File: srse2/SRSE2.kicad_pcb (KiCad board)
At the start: 2 copper layers, 82 x 72 mm, 82 parts, among them J1 s88-N, J2 CAN, P1 I2S, P10 PIC_SPARE, P11 RS485 TERM, P12 RS485, P13 CONN_01X03, P14 CONN_01X04, P15 S88I, P16 CONN_01X04, P17 RA5, P18 CONN_01X03, P19 CONN_01X02, P2 CONN_01X09, P3 CONN_01X02, P4 CONN_01X04, P5 CONN_01X04, P6 ISO_I2C, P7 CAN_TERM, P8 CAN, P9 PIC_I2C, U1 Omega2, U10 OKI-78SR, U2 ADuM1250, U3 MCP2562, U4 PIC18F25K80, U5 HR911105A, U6 SP3485, U8 4504, U9 7812, Y1 16MHz

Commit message: add bulge
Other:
- outline, holes or cut-outs redrawn
- board text added: "V1.5"
- board text removed: "V1.4"
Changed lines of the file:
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@@
-(kicad_pcb (version 4) (host pcbnew 4.0.2+dfsg1-stable)
+(kicad_pcb (version 4) (host pcbnew 4.0.7)
   (general
     (links 208)
     (no_connects 0)
-    (area 97.888667 73.924999 207 154.126)
+    (area 97.963667 73.924999 206.85 154.286)
     (thickness 1.6)
-    (drawings 53)
+    (drawings 56)
     (tracks 1381)
     (zones 0)
@@
     )
   )
+  (gr_arc (start 141 146) (end 141 144) (angle 90) (layer Edge.Cuts) (width 0.15))
+  (gr_arc (start 141 146) (end 139 146) (angle 90) (layer Edge.Cuts) (width 0.15))
+  (gr_line (start 170 146) (end 143 146) (angle 90) (layer Edge.Cuts) (width 0.15))
   (gr_line (start 170 144) (end 170 146) (angle 90) (layer Edge.Cuts) (width 0.15))
   (gr_arc (start 182 144) (end 170 144) (angle 90) (layer Edge.Cuts) (width 0.15))
@@
     (effects (font (size 1 1) (thickness 0.2)))
   )
-  (gr_text V1.4 (at 162.2425 76.0095) (layer F.Cu)
+  (gr_text V1.5 (at 162.2425 76.0095) (layer F.Cu)
     (effects (font (size 1.5 1.5) (thickness 0.3)))
   )
@@
   (gr_line (start 100 86) (end 100 132) (angle 90) (layer Edge.Cuts) (width 0.15))
   (gr_line (start 182 86) (end 182 132) (angle 90) (layer Edge.Cuts) (width 0.15))
-  (gr_line (start 112 146) (end 170 146) (angle 90) (layer Edge.Cuts) (width 0.15))
+  (gr_line (start 112 146) (end 139 146) (angle 90) (layer Edge.Cuts) (width 0.15))
   (gr_arc (start 182 74) (end 182 86) (angle 90) (layer Edge.Cuts) (width 0.15))
   (gr_arc (start 100 74) (end 112 74) (angle 90) (layer Edge.Cuts) (width 0.15))

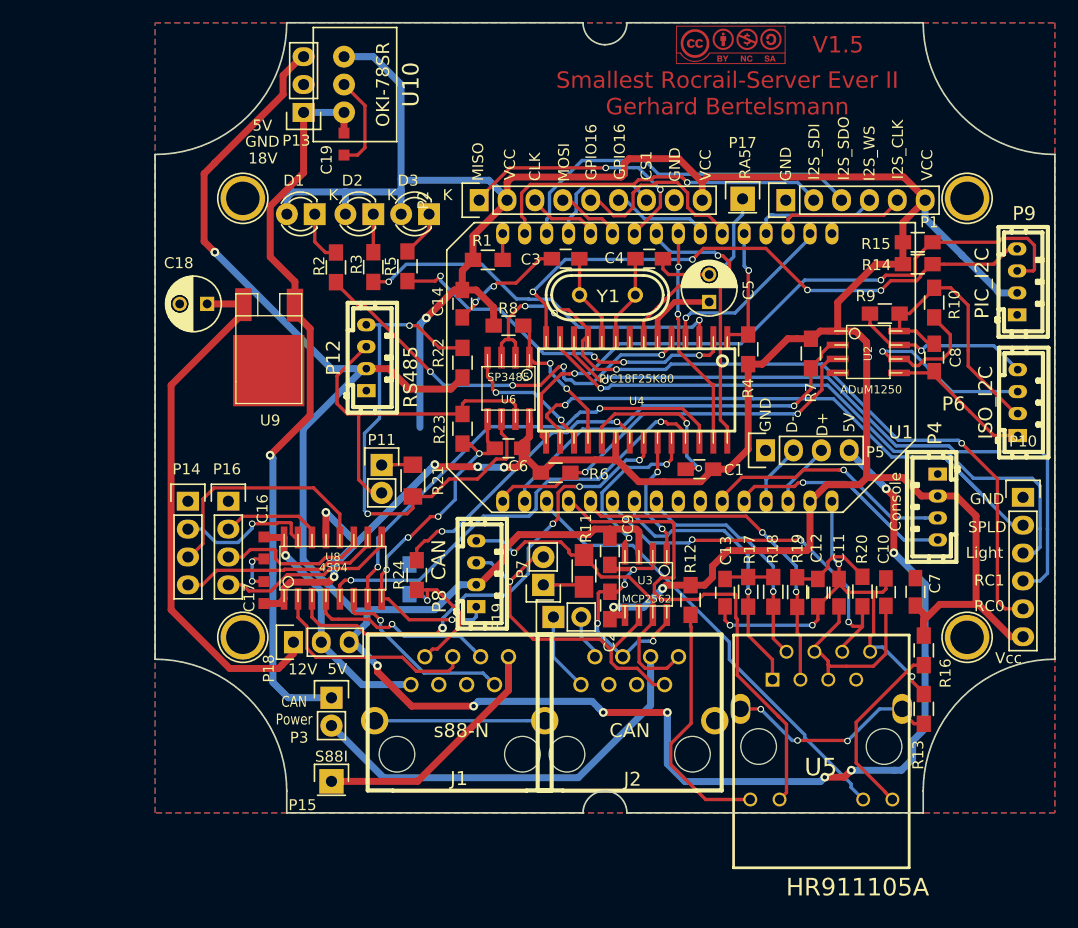
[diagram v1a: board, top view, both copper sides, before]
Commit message: make V1.6 for JLCPCB Assemly Service
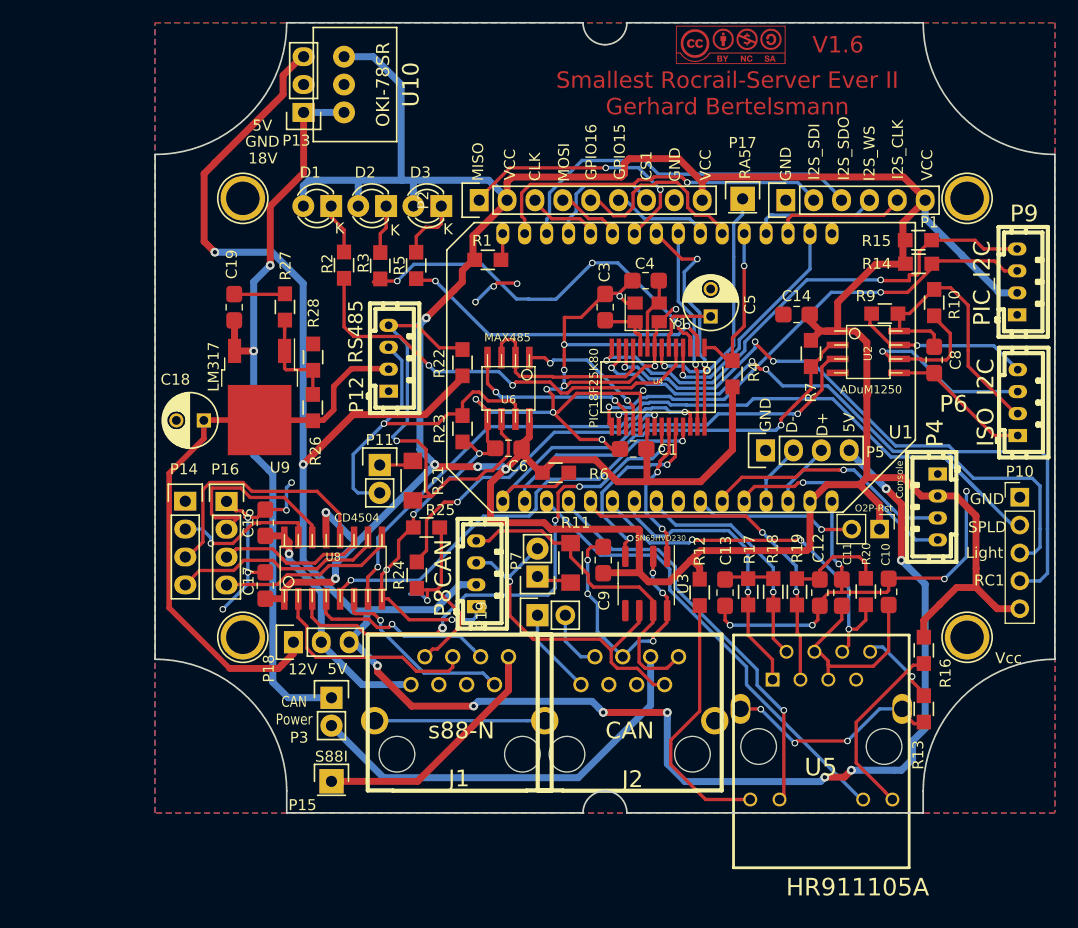
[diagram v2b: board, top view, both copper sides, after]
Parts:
- removed C2, C7: 100nF, Capacitors_SMD:C_0805_HandSoldering
- removed R8: 10k, Resistors_SMD:R_0805_HandSoldering
- added P20: O2P-Rst, Connector_PinHeader_2.54mm:PinHeader_1x02_P2.54mm_Vertical_NB, F.Cu at (166.0, 120.1)
- added R26: 240, Resistors_SMD:R_0805_HandSolderingII, F.Cu at (114.4, 109.1)
- added R27: 2k2, Resistors_SMD:R_0805_HandSolderingII, F.Cu at (111.8, 99.9)
- added R28: 39k, Resistors_SMD:R_0805_HandSolderingII, F.Cu at (114.4, 104.5)
- C3, C4: value 22pF -> 18pF
- P10: footprint Pin_Headers:Pin_Header_Straight_1x06 -> Connector_PinHeader_2.54mm:PinHeader_1x05_P2.54mm_Vertical
- R1, R10, R13, R14, R15, R2, R24, R3, R4, R5, R6, R7, R9: footprint Resistors_SMD:R_0805_HandSoldering -> Resistors_SMD:R_0805_HandSolderingII
- R11, R21: footprint Resistors_SMD:R_1206 -> Resistors_SMD:R_1206_HandSolderingII
- R12, R16: value 220 -> 270; footprint Resistors_SMD:R_0805_HandSoldering -> Resistors_SMD:R_0805_HandSolderingII
- R17, R18, R19, R20: value 50 -> 49.9; footprint Resistors_SMD:R_0805_HandSoldering -> Resistors_SMD:R_0805_HandSolderingII
- R22, R23: value 1k5 -> 3k3; footprint Resistors_SMD:R_0805_HandSoldering -> Resistors_SMD:R_0805_HandSolderingII
- R25: value 18k -> 47k; footprint Resistors_SMD:R_0805_HandSoldering -> Resistors_SMD:R_0805_HandSolderingII; moved to F.Cu
- U3: value MCP2562 -> SN65HVD230; footprint w_smd_dil:so-8 -> Package_SO:SOIC-8_3.9x4.9mm_P1.27mm
- U4: footprint w_smd_dil:soic-28 -> w_smd_dil:ssop-28
- U6: value SP3485 -> MAX485
- U8: value 4504 -> CD4504
- U9: value 7812 -> LM317; footprint TO_SOT_Packages_SMD:TO-252-2Lead -> Package_TO_SOT_SMD:TO-252-2
- Y1: footprint w_crystal:crystal_hc-49s -> Crystal:Crystal_SMD_3225-4Pin_3.2x2.5mm
- moved C14 30.5 mm to (158.5, 100.6), turned to 0 degrees
- moved C19 17.9 mm to (107.2, 99.9), turned to 270 degrees
- moved C18 10.6 mm to (104.4, 110.2)
- moved U9 8.45 mm to (109.5, 108.1), turned to 270 degrees
- moved C1 6.31 mm to (143.6, 112.8)
- moved C3 5.69 mm to (141.0, 99.9), turned to 90 degrees
- moved R25 4.97 mm to (124.7, 120.0), turned to 180 degrees
- moved Y1 3.95 mm to (144.8, 100.4)
- moved R4 2.65 mm to (152.6, 106.0)
- moved C16 2.30 mm to (110.0, 119.6), turned to 270 degrees
- moved R14 2.19 mm to (169.6, 93.8)
- moved P12 2.03 mm to (121.3, 104.6)
- moved C4 2.02 mm to (144.7, 97.5), turned to 180 degrees
- moved U4 1.97 mm to (145.8, 107.2)
- moved R15 1.96 mm to (169.6, 96.0)
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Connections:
- net Net-(P2-Pad5) renamed /GPIO16
- net Net-(P2-Pad6) renamed /GPIO15
- C18 pad 1: Net-(C18-Pad1) -> /12V
- C9 pad 2: +5V -> VCC
- P10 pad 5: /RC0 -> VCC
- P12 pad 2: +5V -> /12V
- P18 pad 1: Net-(C18-Pad1) -> /12V
- U1 pad 26: Net-(U1-Pad26) -> /O2P_RST
- U3 pad 3: +5V -> VCC
- U3 pad 5: VCC -> Net-(U3-Pad5)
- Y1 pad 2: Net-(C4-Pad1) -> GND
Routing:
- net GND: track 144.7 -> 214.0 mm, vias 19 -> 34
- net /RC0: track 75.0 -> 19.4 mm, vias 4 -> 0
- net /12V: track 0.00 -> 53.7 mm
- net Net-(C18-Pad1): track 48.9 -> 0.00 mm
- net +5V: track 205.3 -> 189.4 mm, vias 9 -> 10
- net VCC: track 315.9 -> 331.0 mm, vias 8 -> 6
- net /I2C_SDA: track 60.2 -> 45.3 mm
- net /O2P_RST: track 0.00 -> 14.9 mm, vias 0 -> 1
- net Net-(R26-Pad1): track 0.00 -> 10.1 mm
- net Net-(P16-Pad2): track 9.31 -> 18.4 mm
- net /LLEDG: track 47.0 -> 38.2 mm, vias 0 -> 1
- net /SPI_DO: track 56.3 -> 48.2 mm
- net Net-(R6-Pad1): track 37.3 -> 44.8 mm, vias 2 -> 1
- net /S88_DATA: track 13.2 -> 19.5 mm
- net Net-(P12-Pad4): track 48.1 -> 41.9 mm, vias 2 -> 1
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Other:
- board text added: "GPIO15"
- board text added: "V1.6"
- board text removed: "RC0"
- board text removed: "V1.5"

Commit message: new JLCPCB assembly version V1.7
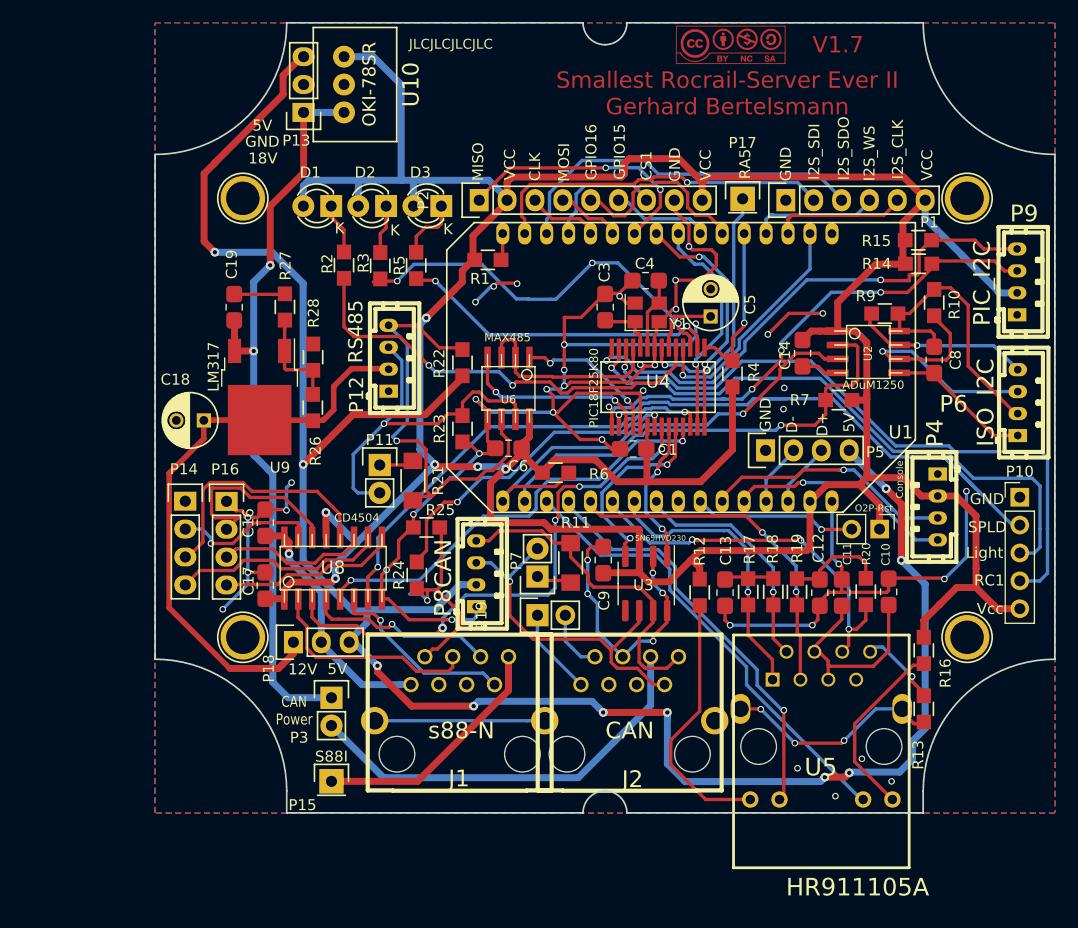
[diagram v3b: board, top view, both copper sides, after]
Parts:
- moved R7 4.94 mm to (162.3, 108.4), turned to 0 degrees
- moved C14 3.57 mm to (159.0, 104.1), turned to 90 degrees
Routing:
- net GND: track 214.0 -> 241.9 mm, vias 34 -> 46
- net Net-(R7-Pad1): track 36.9 -> 42.6 mm
- net /RxD: track 18.3 -> 20.9 mm
- net /RC1: track 60.8 -> 59.2 mm, vias 3 -> 1
- net /SPI_DO: track 48.2 -> 49.7 mm
- net /LIGHT: track 55.5 -> 54.2 mm, vias 3 -> 1
- net /I2C_SDA: track 45.3 -> 46.6 mm, vias 2 -> 4
- net /TxD: track 21.9 -> 22.8 mm
- net Net-(C3-Pad1): track 6.08 -> 5.42 mm
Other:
- board text added: "JLCJLCJLCJLC"
- board text added: "V1.7"
- board text removed: "V1.6"

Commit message: add missing files
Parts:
- removed P14, P16: CONN_01X04, Pin_Headers:Pin_Header_Straight_1x04
- added C100: 10uF, Capacitor_SMD:C_1206_3216Metric_Pad1.33x1.80mm_HandSolder, F.Cu at (103.1, 91.8)
- added C101: 10n, Capacitor_SMD:C_0603_1608Metric_Pad1.08x0.95mm_HandSolder, F.Cu at (103.5, 114.6)
- added C102: 220uF, Capacitor_Tantalum_SMD:CP_EIA-7343-31_Kemet-D_Pad2.25x2.55mm_HandSolder, F.Cu at (112.6, 107.0)
- added D100: SS54, Diode_SMD:D_SMA, F.Cu at (117.1, 96.8)
- added L100: 18uH, Inductor_SMD:L_10.4x10.4_H4.8, F.Cu at (106.6, 99.1)
- added R100: 100k, Resistor_SMD:R_0603_1608Metric, F.Cu at (93.1, 96.5)
- added R101: 10k, Resistor_SMD:R_0603_1608Metric_Pad0.98x0.95mm_HandSolder, F.Cu at (90.1, 112.3)
- added R102: 5k6, Resistor_SMD:R_0603_1608Metric_Pad0.98x0.95mm_HandSolder, F.Cu at (94.3, 112.0)
- added R103: 270, Resistor_SMD:R_0603_1608Metric_Pad0.98x0.95mm_HandSolder, F.Cu at (93.9, 114.6)
- added R104: 0, Resistor_SMD:R_1206_3216Metric_Pad1.30x1.75mm_HandSolder, F.Cu at (103.1, 87.5)
- added R105: 0, Resistor_SMD:R_1206_3216Metric_Pad1.30x1.75mm_HandSolder, F.Cu at (115.8, 91.1)
- added U7: TPS5430DDA, Package_SO:TI_SO-PowerPAD-8_ThermalVias, F.Cu at (103.4, 108.5)
- C18, C5: footprint Capacitors_ThroughHole:C_Radial_D5_L6_P2.5 -> Capacitor_SMD:C_1206_3216Metric_Pad1.33x1.80mm_HandSolder
- moved C18 20.5 mm to (102.8, 130.7), turned to 0 degrees
- moved C19 19.6 mm to (101.0, 118.5), turned to 90 degrees
- moved R27 17.0 mm to (113.4, 116.8), turned to 0 degrees
- moved R2 16.8 mm to (134.0, 97.0)
- moved R26 15.7 mm to (110.3, 124.3)
- moved R28 15.6 mm to (110.4, 119.6), turned to 90 degrees
- moved U9 14.1 mm to (105.6, 121.7)
- moved R3 11.2 mm to (130.8, 100.8), turned to 180 degrees
- moved D1 10.4 mm to (125.2, 95.7)
- moved R5 6.89 mm to (130.4, 98.2), turned to 180 degrees
- moved D2 6.85 mm to (126.0, 86.0)
- moved R24 6.46 mm to (122.8, 118.0), turned to 180 degrees
- moved R25 3.87 mm to (127.6, 117.4)
- moved C16 3.80 mm to (113.8, 119.8)
- moved U8 3.61 mm to (119.8, 123.7)
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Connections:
- net //MCLR renamed //MCLR
- net /LP4 renamed /LP4/5
- net /RC0 renamed /RS485_DE
- J1 pad 9: Net-(J1-Pad9) -> unconnected-(J1-Pad9)
- J2 pad 3: Net-(J2-Pad3) -> unconnected-(J2-Pad3)
- J2 pad 5: Net-(J2-Pad5) -> unconnected-(J2-Pad5)
- J2 pad 9: Net-(J2-Pad9) -> unconnected-(J2-Pad9)
- U1 pad 25: Net-(U1-Pad25) -> unconnected-(U1-Pad25)
- U3 pad 5: Net-(U3-Pad5) -> unconnected-(U3-Pad5)
- U5 pad 7: Net-(U5-Pad7) -> unconnected-(U5-Pad7)
- U8 pad 10: Net-(P14-Pad4) -> unconnected-(U8-Pad10)
- U8 pad 11: Net-(P16-Pad3) -> unconnected-(U8-Pad11)
- U8 pad 12: Net-(P14-Pad3) -> unconnected-(U8-Pad12)
- U8 pad 14: Net-(P16-Pad2) -> unconnected-(U8-Pad14)
- U8 pad 15: Net-(P14-Pad2) -> unconnected-(U8-Pad15)
- U8 pad 9: Net-(P16-Pad4) -> unconnected-(U8-Pad9)
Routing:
- net +5V: track 189.4 -> 107.5 mm, vias 10 -> 8
- net VCC: track 331.2 -> 260.1 mm, vias 6 -> 3
- net +24V: track 68.7 -> 9.61 mm, vias 2 -> 0
- net /12V: track 53.7 -> 7.40 mm
- net GND: track 241.9 -> 199.9 mm, vias 46 -> 36
- net Net-(P12-Pad4): track 41.9 -> 10.5 mm, vias 1 -> 0
- net Net-(P11-Pad2): track 33.3 -> 8.05 mm, vias 1 -> 0
- net Net-(P14-Pad3): track 22.8 -> 0.00 mm
- net Net-(R2-Pad2): track 39.9 -> 19.9 mm, vias 2 -> 1
- net Net-(P14-Pad4): track 19.5 -> 0.00 mm
- net Net-(P16-Pad2): track 18.4 -> 0.00 mm
- net Net-(P16-Pad4): track 16.3 -> 0.00 mm
- net unconnected-(J1-Pad9): track 0.00 -> 15.5 mm
- net Net-(J1-Pad9): track 15.5 -> 0.00 mm
- net Net-(P16-Pad3): track 14.6 -> 0.00 mm
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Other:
- net class Default removed
- net class Power removed
- net class double removed
- board text added: "Smallest Railroad-Server Ever II Gerhard Bertelsmann"
- board text added: "V1.8"
- board text removed: "Smallest Rocrail-Server Ever II Gerhard Bertelsmann"
- board text removed: "V1.7"

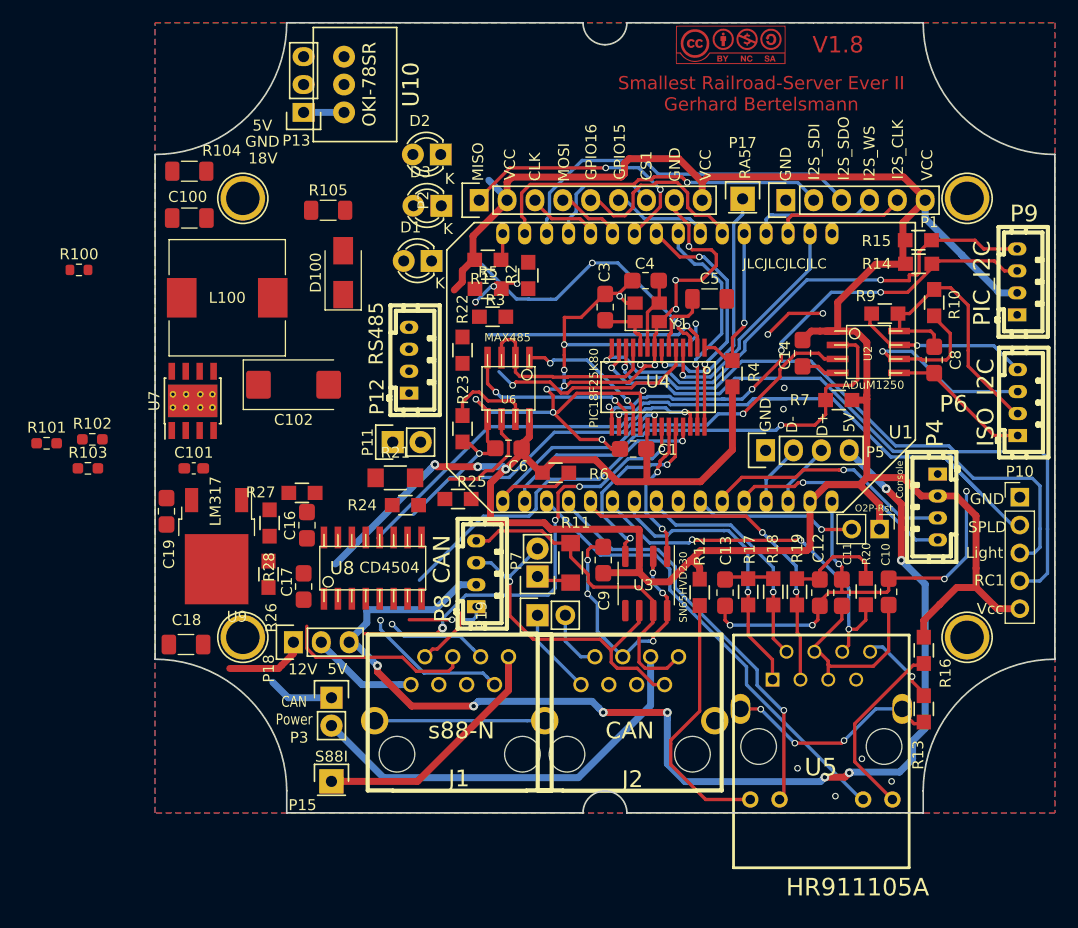
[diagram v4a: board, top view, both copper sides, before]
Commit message: move components to satisfy DCDC requirements
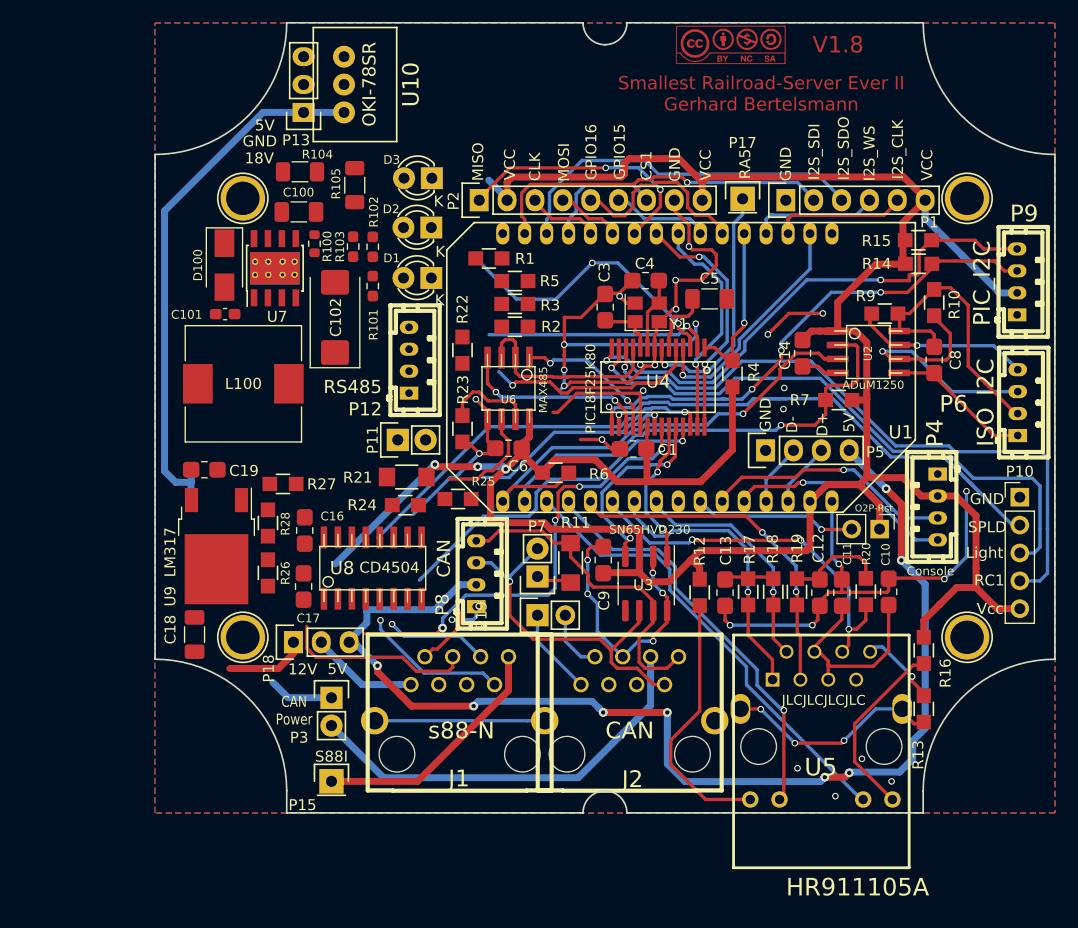
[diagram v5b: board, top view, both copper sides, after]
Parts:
- moved R101 33.0 mm to (119.8, 98.0), turned to 90 degrees
- moved R103 31.5 mm to (118.0, 94.4), turned to 90 degrees
- moved R102 31.0 mm to (119.8, 94.4), turned to 90 degrees
- moved R100 21.6 mm to (114.5, 94.1), turned to -90 degrees
- moved C101 14.3 mm to (106.4, 100.5), turned to 180 degrees
- moved U7 14.2 mm to (110.9, 96.4)
- moved D100 10.8 mm to (106.3, 96.1), turned to -90 degrees
- moved R104 10.1 mm to (113.2, 87.6)
- moved C100 10.00 mm to (113.1, 91.2)
- moved L100 7.98 mm to (108.0, 106.9)
- moved C102 7.20 mm to (116.4, 100.8), turned to 90 degrees
- moved D2 6.71 mm to (125.2, 92.7)
- moved C19 5.12 mm to (104.5, 114.7), turned to 180 degrees
- moved R2 4.83 mm to (132.8, 101.7), turned to 0 degrees
- moved R105 3.33 mm to (118.2, 88.8), turned to 90 degrees
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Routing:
- net +24V: track 9.61 -> 55.3 mm
- net GND: track 199.9 -> 181.3 mm, vias 36 -> 34
- net VCC: track 260.1 -> 250.1 mm
- net Net-(D3-Pad1): track 4.73 -> 0.00 mm, vias 3 -> 0
- net Net-(R1-Pad2): track 2.40 -> 0.02 mm
